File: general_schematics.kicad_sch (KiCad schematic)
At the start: 0 parts

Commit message: made additions to the project
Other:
- added sheet atmega2560 (atmega2560.kicad_sch)
- added sheet basic components (basic components.kicad_sch)
- added sheet voltageRegulator (voltageRegulator.kicad_sch)

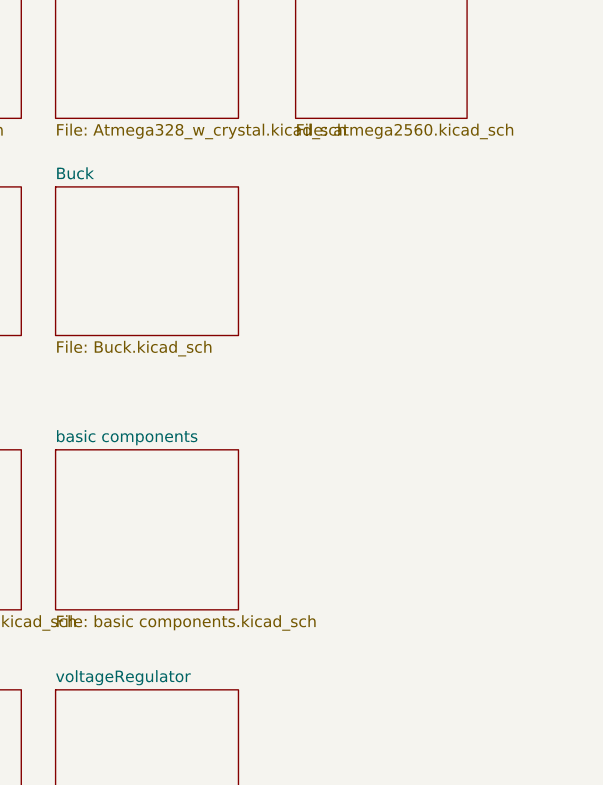
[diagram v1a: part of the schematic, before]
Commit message: added ch340.sch
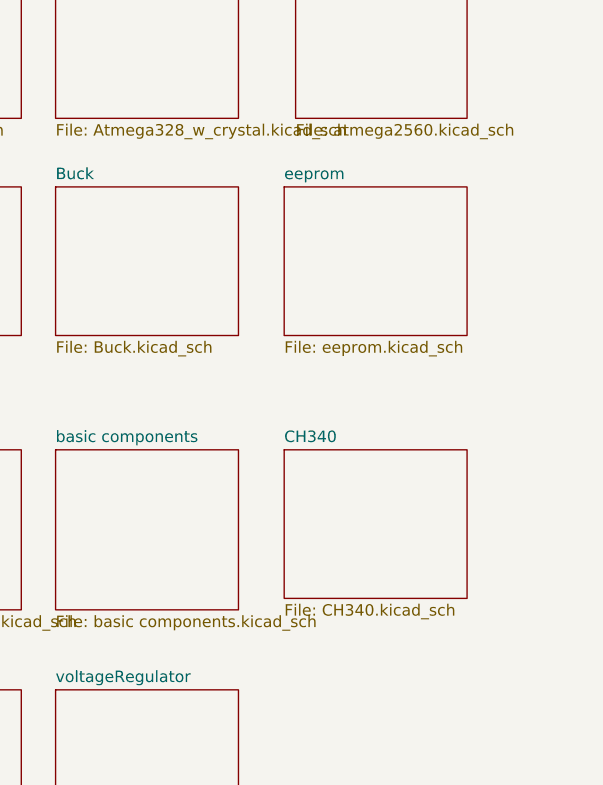
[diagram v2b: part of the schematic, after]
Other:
- added sheet CH340 (CH340.kicad_sch)
- added sheet eeprom (eeprom.kicad_sch)

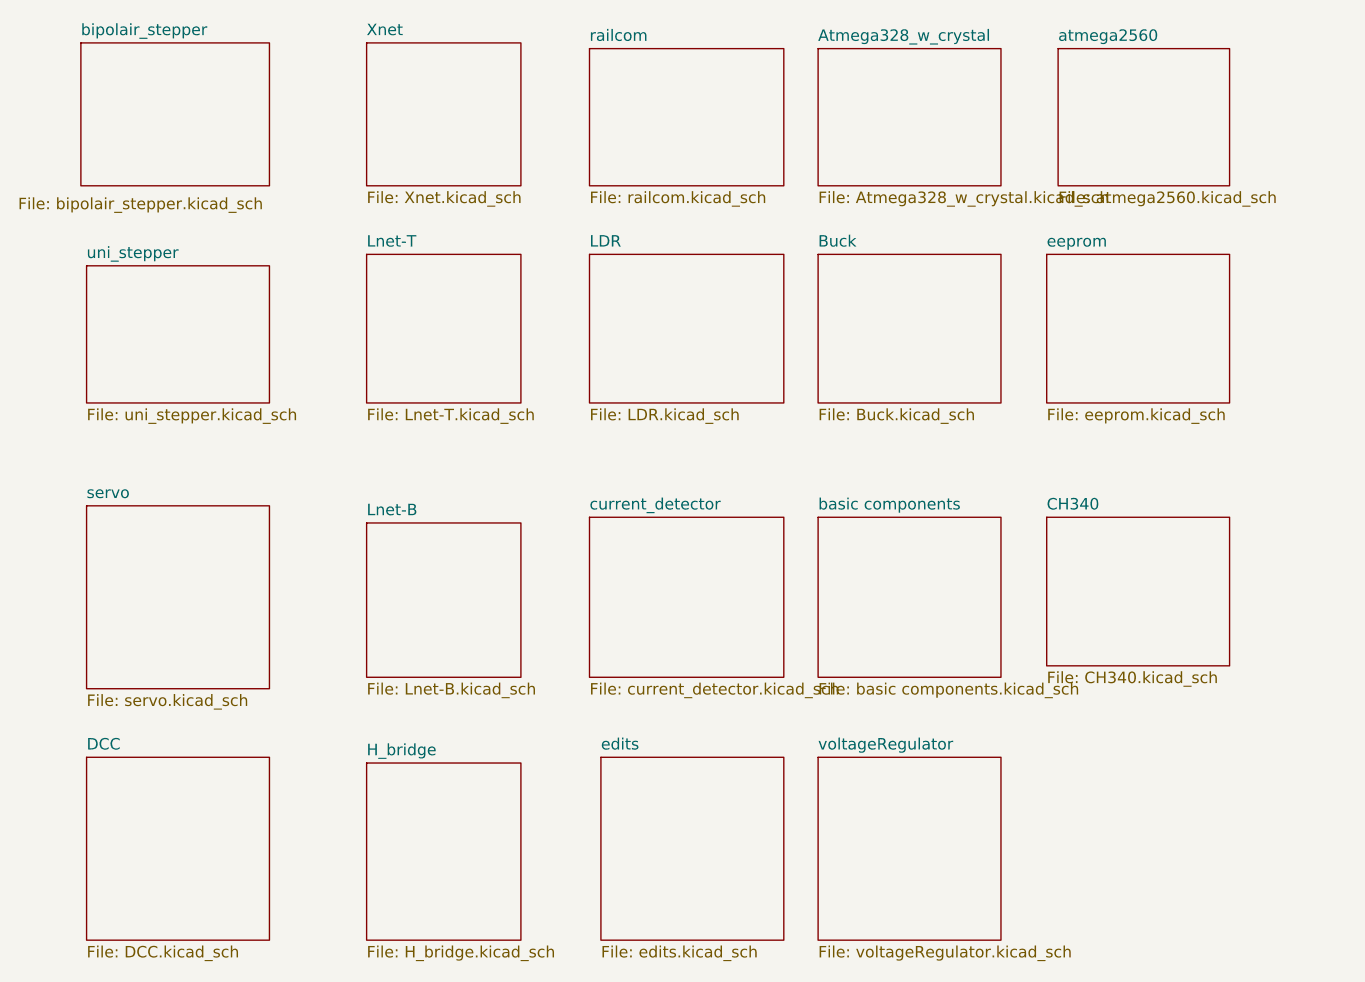
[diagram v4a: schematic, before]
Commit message: added hierarchial labels to some schematics
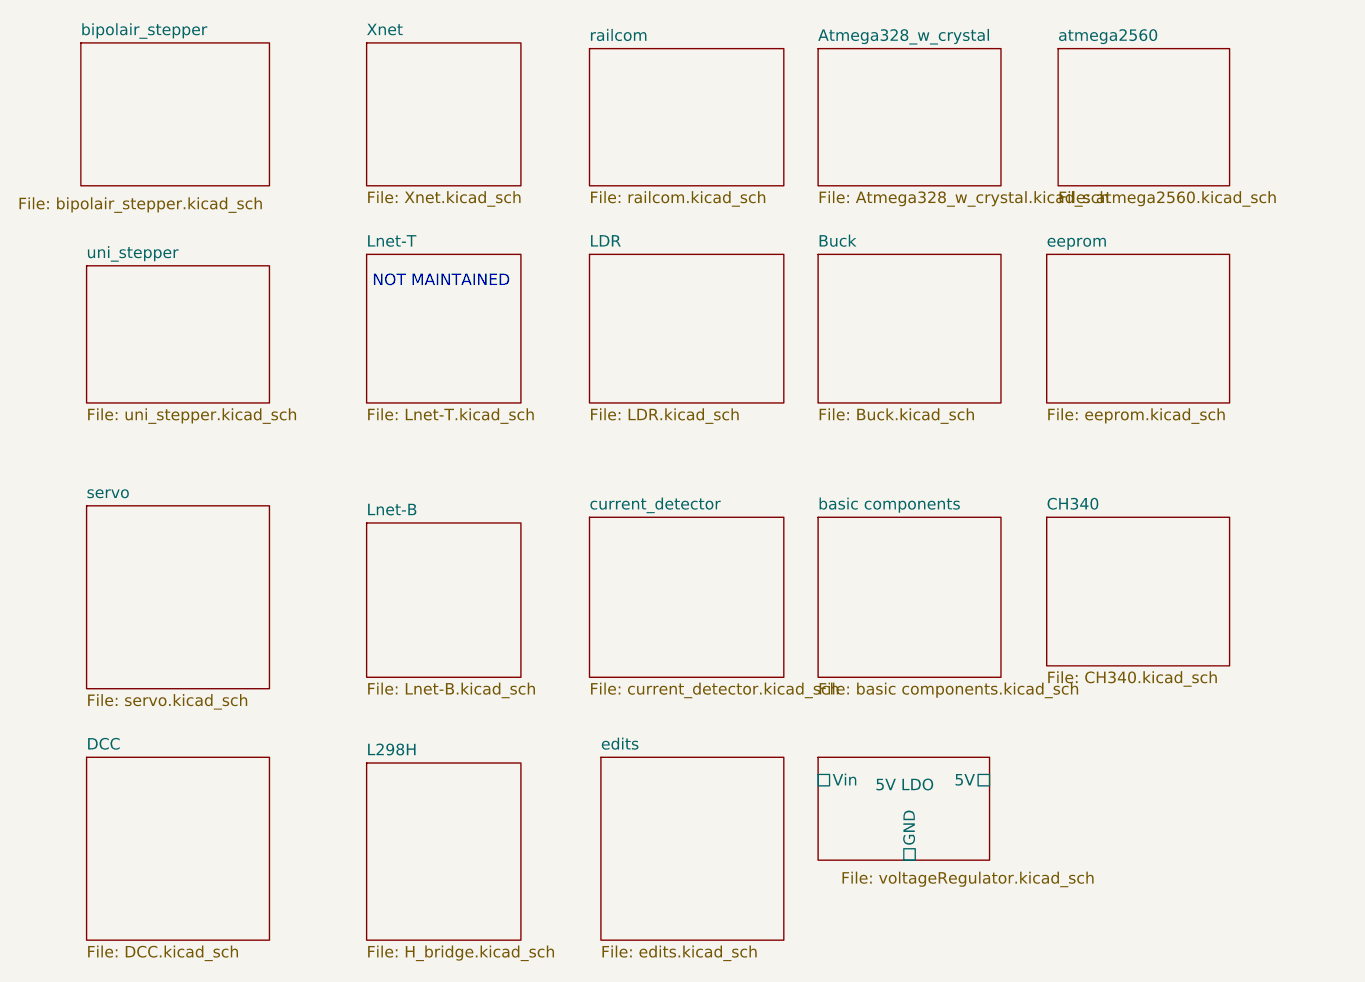
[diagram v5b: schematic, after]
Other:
- sheet H_bridge renamed L298H
- sheet voltageRegulator renamed 5V LDO
- sheet 5V LDO ports: added 5V, GND, Vin; removed none
- note added: "NOT MAINTAINED"

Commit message: moved some schematic scheets to their own folders and routed a board with it. This allow for re-use of PCB parts.
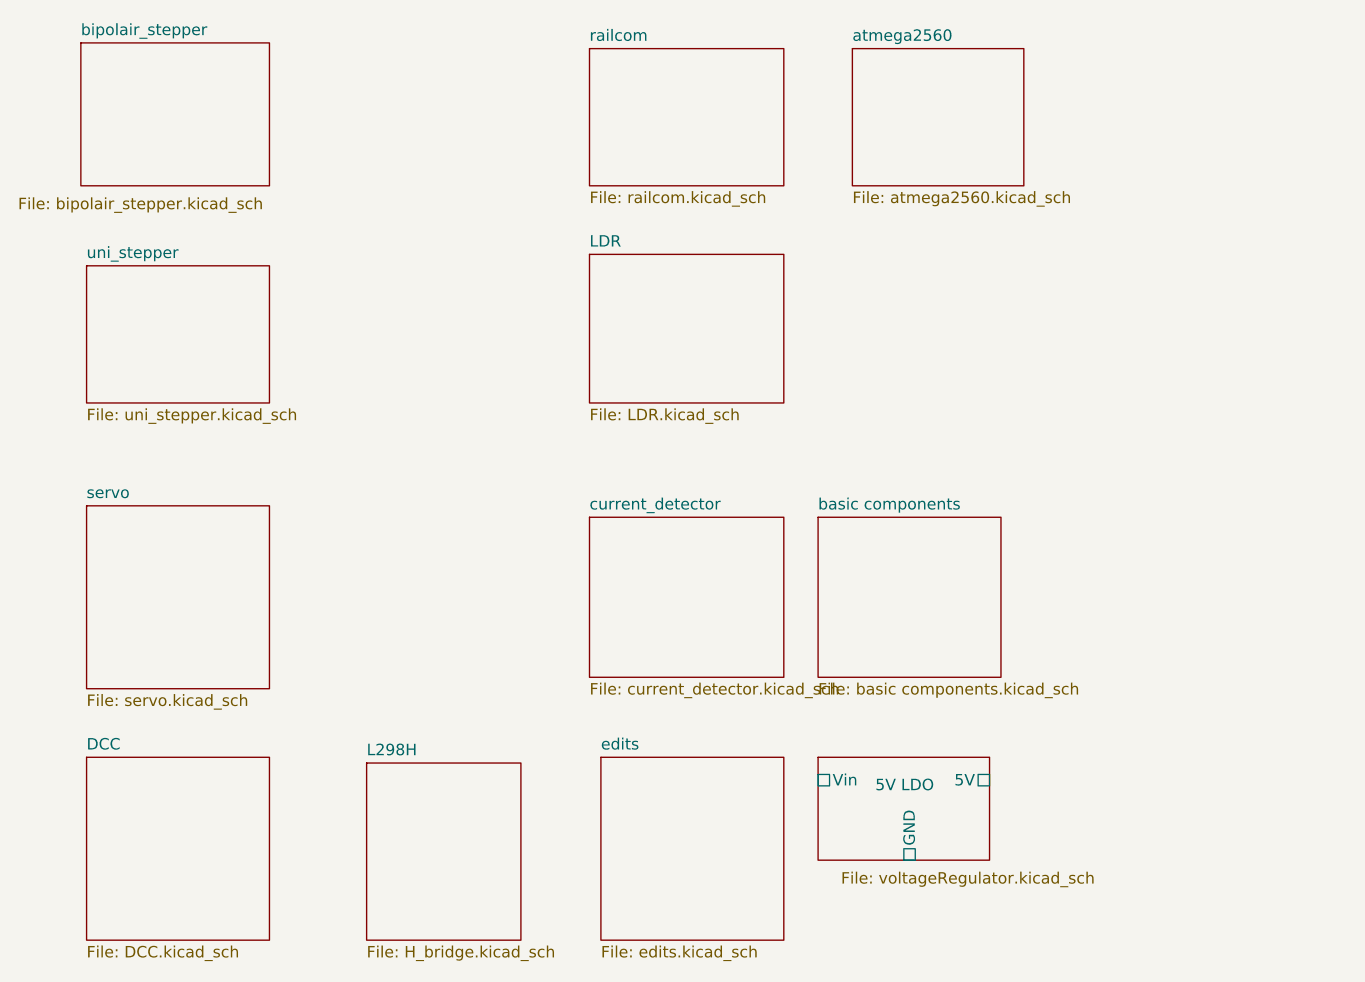
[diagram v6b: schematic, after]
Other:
- removed sheet Atmega328_w_crystal
- removed sheet Buck
- removed sheet CH340
- removed sheet Lnet-B
- removed sheet Lnet-T
- removed sheet Xnet
- removed sheet eeprom
- note removed: "NOT MAINTAINED"
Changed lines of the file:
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@@
 (kicad_sch (version 20230121) (generator eeschema)
   (paper "A4")
-  (text "NOT MAINTAINED" (at 99.06 59.69 0)
-    (effects (font (size 1.27 1.27)) (justify left bottom))
-  )
-  (sheet (at 173.99 55.88) (size 20.32 16.51) (fields_autoplaced)
-    (stroke (width 0.1524) (type solid))
-    (fill (color 0 0 0 0.0000))
-    (property "Sheetname" "eeprom" (at 173.99 55.1684 0)
-      (effects (font (size 1.27 1.27)) (justify left bottom))
-    )
-    (property "Sheetfile" "eeprom.kicad_sch" (at 173.99 72.9746 0)
-      (effects (font (size 1.27 1.27)) (justify left top))
-    )
-    (instances
-      (project "general_schematics"
-        (path "/e777d9ec-d073-4229-a9e6-2cf85636e407" (page "19"))
-      )
-    )
-  )
   (sheet (at 148.59 85.09) (size 20.32 17.78) (fields_autoplaced)
     (stroke (width 0.1524) (type solid))
@@
       (project "general_schematics"
         (path "/e777d9ec-d073-4229-a9e6-2cf85636e407" (page "16"))
-      )
-    )
-  )
-  (sheet (at 98.425 85.725) (size 17.145 17.145) (fields_autoplaced)
-    (stroke (width 0.1524) (type solid))
-    (fill (color 0 0 0 0.0000))
-    (property "Sheetname" "Lnet-B" (at 98.425 85.0134 0)
-      (effects (font (size 1.27 1.27)) (justify left bottom))
-    )
-    (property "Sheetfile" "Lnet-B.kicad_sch" (at 98.425 103.4546 0)
-      (effects (font (size 1.27 1.27)) (justify left top))
-    )
-    (instances
-      (project "general_schematics"
-        (path "/e777d9ec-d073-4229-a9e6-2cf85636e407" (page "6"))
-      )
-    )
-  )
-  (sheet (at 98.425 32.385) (size 17.145 15.875) (fields_autoplaced)
-    (stroke (width 0.1524) (type solid))
-    (fill (color 0 0 0 0.0000))
-    (property "Sheetname" "Xnet" (at 98.425 31.6734 0)
-      (effects (font (size 1.27 1.27)) (justify left bottom))
-    )
-    (property "Sheetfile" "Xnet.kicad_sch" (at 98.425 48.8446 0)
-      (effects (font (size 1.27 1.27)) (justify left top))
-    )
-    (instances
-      (project "general_schematics"
-        (path "/e777d9ec-d073-4229-a9e6-2cf85636e407" (page "4"))
       )
     )
@@
     )
   )
-  (sheet (at 148.59 55.88) (size 20.32 16.51) (fields_autoplaced)
-    (stroke (width 0.1524) (type solid))
-    (fill (color 0 0 0 0.0000))
-    (property "Sheetname" "Buck" (at 148.59 55.1684 0)
-      (effects (font (size 1.27 1.27)) (justify left bottom))
-    )
-    (property "Sheetfile" "Buck.kicad_sch" (at 148.59 72.9746 0)
-      (effects (font (size 1.27 1.27)) (justify left top))
-    )
-    (instances
-      (project "general_schematics"
-        (path "/e777d9ec-d073-4229-a9e6-2cf85636e407" (page "15"))
-      )
-    )
-  )
   (sheet (at 98.425 112.395) (size 17.145 19.685) (fields_autoplaced)
     (stroke (width 0.1524) (type solid))
@@
     )
   )
-  (sheet (at 98.425 55.88) (size 17.145 16.51) (fields_autoplaced)
-    (stroke (width 0.1524) (type solid))
-    (fill (color 0 0 0 0.0000))
-    (property "Sheetname" "Lnet-T" (at 98.425 55.1684 0)
-      (effects (font (size 1.27 1.27)) (justify left bottom))
-    )
-    (property "Sheetfile" "Lnet-T.kicad_sch" (at 98.425 72.9746 0)
-      (effects (font (size 1.27 1.27)) (justify left top))
-    )
-    (instances
-      (project "general_schematics"
-        (path "/e777d9ec-d073-4229-a9e6-2cf85636e407" (page "5"))
-      )
-    )
-  )
   (sheet (at 124.46 111.76) (size 20.32 20.32) (fields_autoplaced)
     (stroke (width 0.1524) (type solid))
@@
     )
   )
-  (sheet (at 175.26 33.02) (size 19.05 15.24) (fields_autoplaced)
+  (sheet (at 152.4 33.02) (size 19.05 15.24) (fields_autoplaced)
     (stroke (width 0.1524) (type solid))
     (fill (color 0 0 0 0.0000))
-    (property "Sheetname" "atmega2560" (at 175.26 32.3084 0)
+    (property "Sheetname" "atmega2560" (at 152.4 32.3084 0)
       (effects (font (size 1.27 1.27)) (justify left bottom))
     )
-    (property "Sheetfile" "atmega2560.kicad_sch" (at 175.26 48.8446 0)
+    (property "Sheetfile" "atmega2560.kicad_sch" (at 152.4 48.8446 0)
       (effects (font (size 1.27 1.27)) (justify left top))
     )
@@
       )
     )
-  )
-  (sheet (at 173.99 85.09) (size 20.32 16.51) (fields_autoplaced)
-    (stroke (width 0.1524) (type solid))
-    (fill (color 0 0 0 0.0000))
-    (property "Sheetname" "CH340" (at 173.99 84.3784 0)
-      (effects (font (size 1.27 1.27)) (justify left bottom))
-    )
-    (property "Sheetfile" "CH340.kicad_sch" (at 173.99 102.1846 0)
-      (effects (font (size 1.27 1.27)) (justify left top))
-    )
-    (instances
-      (project "general_schematics"
-        (path "/e777d9ec-d073-4229-a9e6-2cf85636e407" (page "20"))
-      )
-    )
-  )
-  (sheet (at 148.59 33.02) (size 20.32 15.24) (fields_autoplaced)
-    (stroke (width 0.1524) (type solid))
-    (fill (color 0 0 0 0.0000))
-    (property "Sheetname" "Atmega328_w_crystal" (at 148.59 32.3084 0)
-      (effects (font (size 1.27 1.27)) (justify left bottom))
-    )
-    (property "Sheetfile" "Atmega328_w_crystal.kicad_sch" (at 148.59 48.8446 0)
-      (effects (font (size 1.27 1.27)) (justify left top))
-    )
-    (instances
-      (project "general_schematics"
-        (path "/e777d9ec-d073-4229-a9e6-2cf85636e407" (page "14"))
-      )
-    )
